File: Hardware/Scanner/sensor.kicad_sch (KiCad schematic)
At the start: 22 parts, among them U1 OPA2376xxD, U4 OPA2376xxD

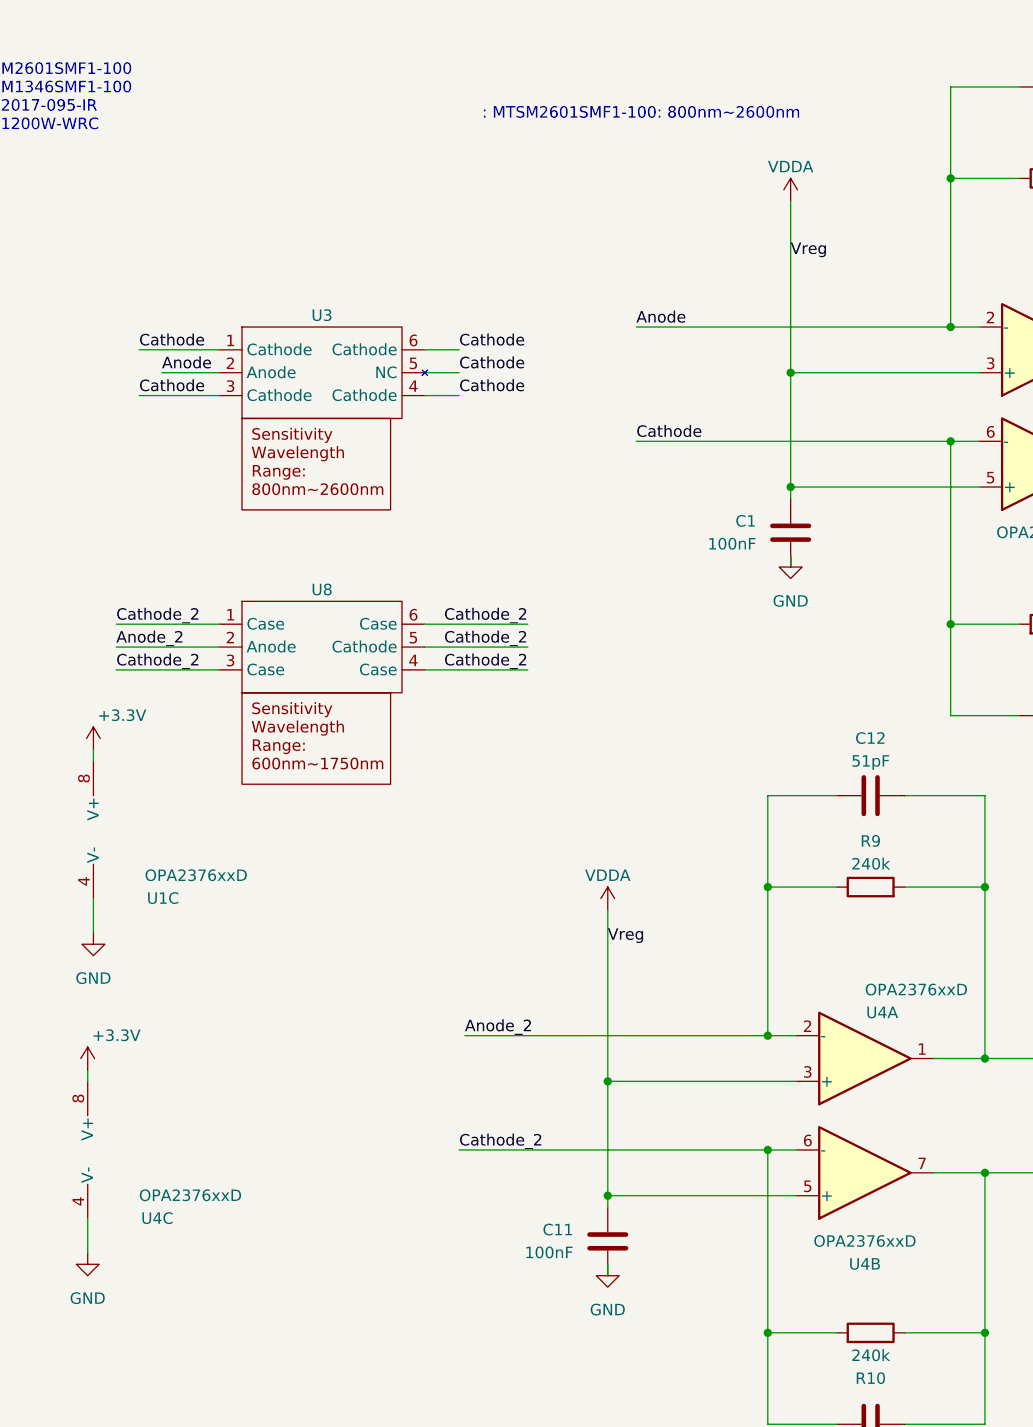
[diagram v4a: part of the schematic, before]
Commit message: updated schematic, and layout, updated bom, fully converted to 3.3v for Voltage input only
Signed-off-by: lokimetasmith <lokimail@gmail.com>
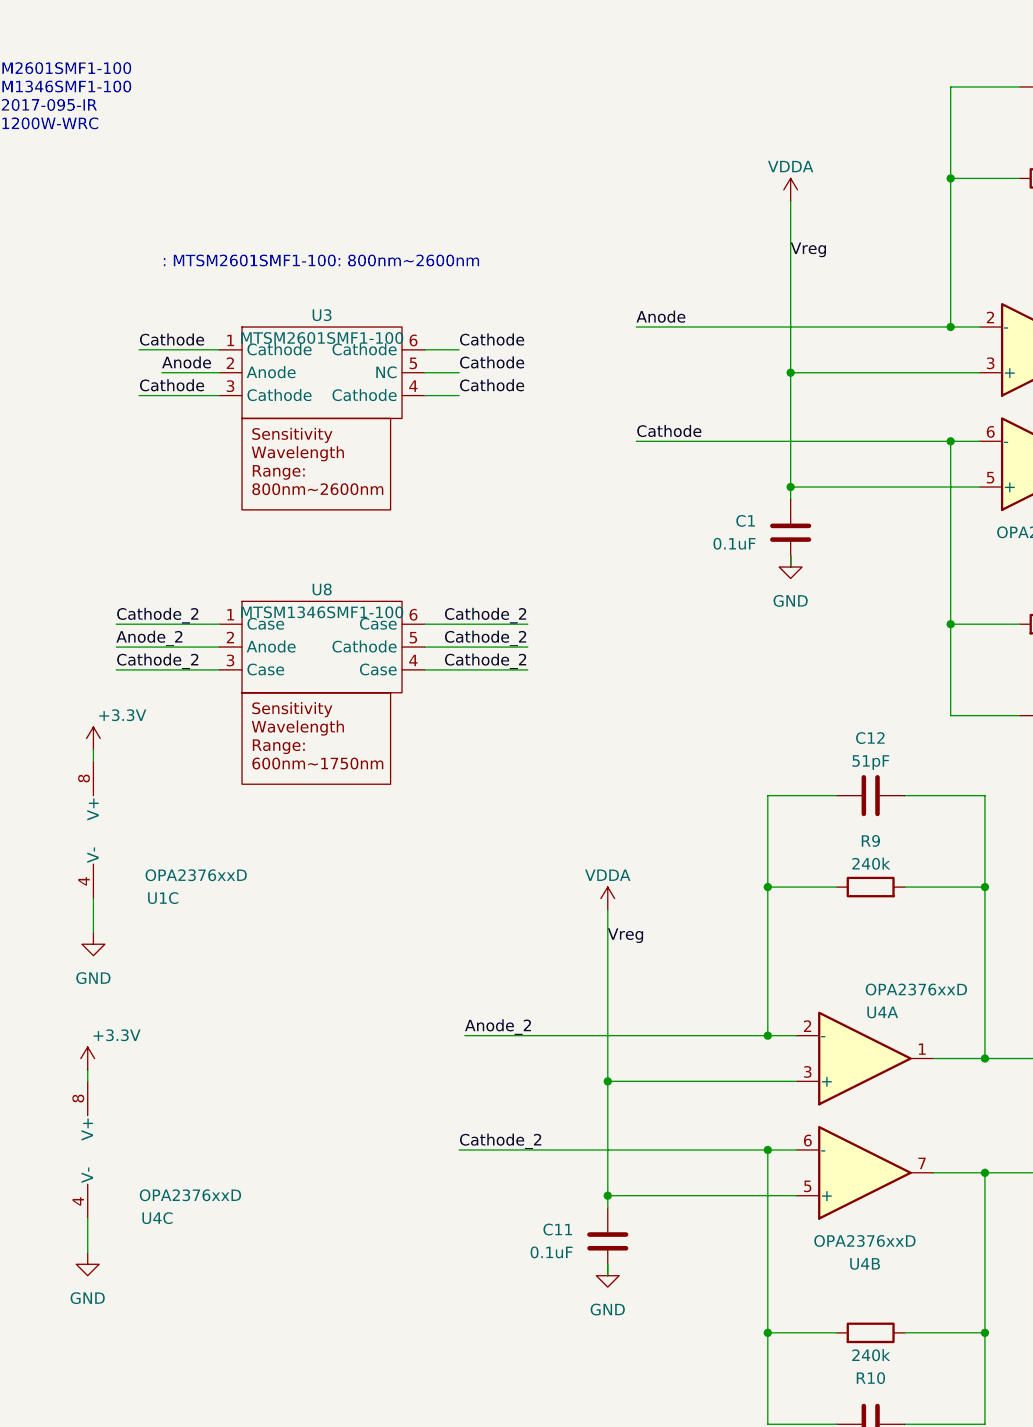
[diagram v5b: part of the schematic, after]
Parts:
- C1, C11: value 100nF -> 0.1uF; digikey description (none) -> CAP CER 0.1UF 16V X7R 0603; digikey part number (none) -> 311-1088-1-ND
- C12, C2, C21, C3: digikey description (none) -> CAP CER 51PF 50V C0G/NP0 0603; digikey part number (none) -> 1276-2310-1-ND
- C22, C4: digikey description (none) -> CAP CER 0.047UF 50V X7R 0603; digikey part number (none) -> 311-4019-1-ND
- C23, C5: digikey description (none) -> CAP CER 100PF 50V C0G/NP0 0603; digikey part number (none) -> 1276-1008-1-ND
- R1, R10, R2, R9: digikey description (none) -> RES 240K OHM 1% 1/10W 0603; digikey part number (none) -> 311-240KHRCT-ND; mouser description (none) -> ERJ-3EKF2403V; mouser part number (none) -> 667-ERJ-3EKF2403V
- R13, R14, R3, R4: digikey description (none) -> RES SMD 301 OHM 1% 1/10W 0603; digikey part number (none) -> P301HCT-ND; mouser description (none) -> ERJ-3EKF3010V; mouser part number (none) -> 667-ERJ-3EKF3010V
- U1, U4: digikey description (none) -> General Purpose Amplifier 2 Circuit Single Ended, Rail-to-R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; mouser description (none) -> OPA2376AIDR; mouser part number (none) -> 595-OPA2376AIDR
- U3: value ~ -> MTSM2601SMF1-100; digikey description (none) -> SENSOR PHOTODIODE 800-2600NM SMD; digikey part number (none) -> 1125-MTSM2601SMF1-100-ND
- U8: value ~ -> MTSM1346SMF1-100; digikey description (none) -> SENSOR PHOTODIODE 1300NM 6SMD; digikey part number (none) -> 1125-MTSM1346SMF1-100-ND

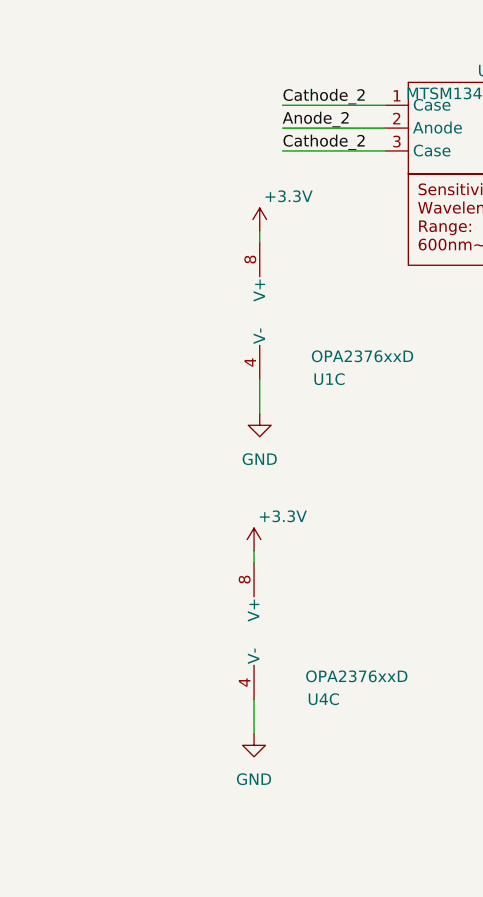
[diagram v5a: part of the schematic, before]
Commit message: added decoupling capactitors, added footprint for 3d model, need to verify new footprint
Signed-off-by: lokimetasmith <lokimail@gmail.com>
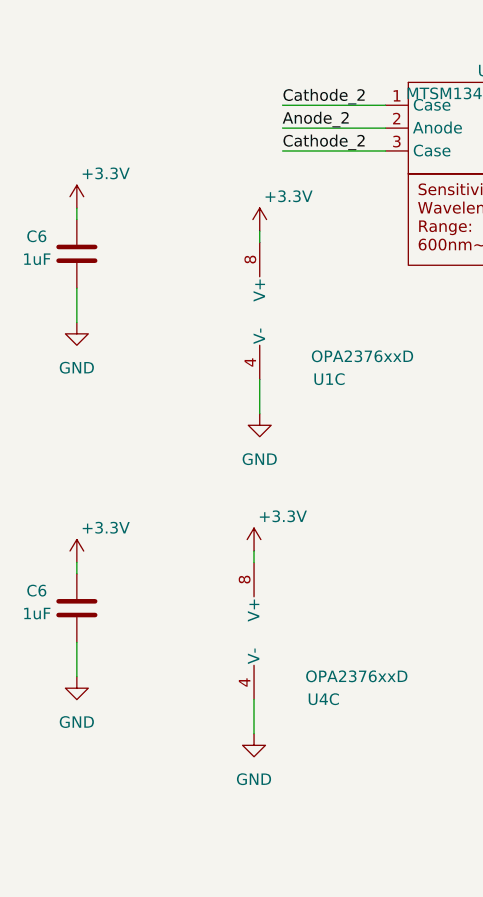
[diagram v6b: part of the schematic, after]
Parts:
- added C6 (x2): 1uF, Capacitor_SMD:C_0603_1608Metric_Pad1.08x0.95mm_HandSolder, symbol Device:C
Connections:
- net +3.3V: now also C6.2, C6.2
- net GND: now also C6.1, C6.1
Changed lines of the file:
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@@
+    (stroke (width 0) (type default))
+  )
+  (wire (pts (xy 17.78 104.14) (xy 17.78 107.95))
     (stroke (width 0) (type default))
   )
@@
     (stroke (width 0) (type default))
   )
+  (wire (pts (xy 17.78 134.62) (xy 17.78 135.89))
+    (stroke (width 0) (type default))
+  )
   (wire (pts (xy 133.35 63.5) (xy 136.525 63.5))
     (stroke (width 0) (type default))
@@
     (stroke (width 0) (type default))
   )
+  (wire (pts (xy 17.78 95.25) (xy 17.78 96.52))
+    (stroke (width 0) (type default))
+  )
   (wire (pts (xy 133.35 83.82) (xy 140.97 83.82))
     (stroke (width 0) (type default))
@@
   )
   (wire (pts (xy 113.03 172.72) (xy 120.65 172.72))
+    (stroke (width 0) (type default))
+  )
+  (wire (pts (xy 17.78 143.51) (xy 17.78 147.32))
     (stroke (width 0) (type default))
   )
@@
     )
   )
+  (symbol (lib_id "Device:C") (at 17.78 100.33 180) (unit 1)
+    (in_bom yes) (on_board yes) (dnp no)
+    (property "Reference" "C6" (at 13.335 98.425 0)
+      (effects (font (size 1.27 1.27)))
+    )
+    (property "Value" "1uF" (at 13.335 100.965 0)
+      (effects (font (size 1.27 1.27)))
+    )
+    (property "Footprint" "Capacitor_SMD:C_0603_1608Metric_Pad1.08x0.95mm_HandSolder" (at 16.8148 96.52 0)
+      (effects (font (size 1.27 1.27)) hide)
+    )
+    (property "Datasheet" "~" (at 17.78 100.33 0)
+      (effects (font (size 1.27 1.27)) hide)
+    )
+    (property "digikey description" "CAP CER 1UF 16V X7R 0603" (at 17.78 100.33 0)
+      (effects (font (size 1.27 1.27)) hide)
+    )
+    (property "digikey part number" "311-1446-1-ND" (at 17.78 100.33 0)
+      (effects (font (size 1.27 1.27)) hide)
+    )
+    (pin "1")
+    (pin "2")
+    (instances
+      (project "RoundScanner"
+        (path "/a818e058-3544-4da8-96fb-1a428660711f/a8dcb7a4-48cf-403e-b881-d44234291c62"
+          (reference "C6") (unit 1)
+        )
+        (path "/a818e058-3544-4da8-96fb-1a428660711f/98df1e87-3735-4cb9-8253-663f6eb2234f"
+          (reference "C24") (unit 1)
+        )
+      )
+    )
+  )
   (symbol (lib_id "Device:R") (at 144.78 83.82 270) (mirror x) (unit 1)
     (in_bom yes) (on_board yes) (dnp no)
@@
         (path "/a818e058-3544-4da8-96fb-1a428660711f/98df1e87-3735-4cb9-8253-663f6eb2234f"
           (reference "R3") (unit 1)
+        )
+      )
+    )
+  )
+  (symbol (lib_id "Device:C") (at 17.78 139.7 180) (unit 1)
+    (in_bom yes) (on_board yes) (dnp no)
+    (property "Reference" "C6" (at 13.335 137.795 0)
+      (effects (font (size 1.27 1.27)))
+    )
+    (property "Value" "1uF" (at 13.335 140.335 0)
+      (effects (font (size 1.27 1.27)))
+    )
+    (property "Footprint" "Capacitor_SMD:C_0603_1608Metric_Pad1.08x0.95mm_HandSolder" (at 16.8148 135.89 0)
+      (effects (font (size 1.27 1.27)) hide)
+    )
+    (property "Datasheet" "~" (at 17.78 139.7 0)
+      (effects (font (size 1.27 1.27)) hide)
+    )
+    (property "digikey description" "CAP CER 1UF 16V X7R 0603" (at 17.78 139.7 0)
+      (effects (font (size 1.27 1.27)) hide)
+    )
+    (property "digikey part number" "311-1446-1-ND" (at 17.78 139.7 0)
+      (effects (font (size 1.27 1.27)) hide)
+    )
+    (pin "1")
+    (pin "2")
+    (instances
+      (project "RoundScanner"
+        (path "/a818e058-3544-4da8-96fb-1a428660711f/a8dcb7a4-48cf-403e-b881-d44234291c62"
+          (reference "C6") (unit 1)
+        )
+        (path "/a818e058-3544-4da8-96fb-1a428660711f/98df1e87-3735-4cb9-8253-663f6eb2234f"
+          (reference "C8") (unit 1)
         )
       )
@@
     )
   )
+  (symbol (lib_id "power:+3.3V") (at 17.78 95.25 0) (unit 1)
+    (in_bom yes) (on_board yes) (dnp no)
+    (property "Reference" "#PWR021" (at 17.78 99.06 0)
+      (effects (font (size 1.27 1.27)) hide)
+    )
+    (property "Value" "+3.3V" (at 20.955 91.44 0)
+      (effects (font (size 1.27 1.27)))
+    )
+    (property "Footprint" "" (at 17.78 95.25 0)
+      (effects (font (size 1.27 1.27)) hide)
+    )
+    (property "Datasheet" "" (at 17.78 95.25 0)
+      (effects (font (size 1.27 1.27)) hide)
+    )
+    (pin "1")
+    (instances
+      (project "RoundScanner"
+        (path "/a818e058-3544-4da8-96fb-1a428660711f/98df1e87-3735-4cb9-8253-663f6eb2234f"
+          (reference "#PWR021") (unit 1)
+        )
+      )
+    )
+  )
+  (symbol (lib_id "power:GND") (at 17.78 107.95 0) (unit 1)
+    (in_bom yes) (on_board yes) (dnp no) (fields_autoplaced)
+    (property "Reference" "#PWR027" (at 17.78 114.3 0)
+      (effects (font (size 1.27 1.27)) hide)
+    )
+    (property "Value" "GND" (at 17.78 113.03 0)
+      (effects (font (size 1.27 1.27)))
+    )
+    (property "Footprint" "" (at 17.78 107.95 0)
+      (effects (font (size 1.27 1.27)) hide)
+    )
+    (property "Datasheet" "" (at 17.78 107.95 0)
+      (effects (font (size 1.27 1.27)) hide)
+    )
+    (pin "1")
+    (instances
+      (project "RoundScanner"
+        (path "/a818e058-3544-4da8-96fb-1a428660711f/98df1e87-3735-4cb9-8253-663f6eb2234f"
+          (reference "#PWR027") (unit 1)
+        )
+      )
+    )
+  )
   (symbol (lib_id "power:GND") (at 95.25 154.94 0) (unit 1)
     (in_bom yes) (on_board yes) (dnp no) (fields_autoplaced)
@@
         (path "/a818e058-3544-4da8-96fb-1a428660711f/98df1e87-3735-4cb9-8253-663f6eb2234f"
           (reference "#PWR09") (unit 1)
+        )
+      )
+    )
+  )
+  (symbol (lib_id "power:+3.3V") (at 17.78 134.62 0) (unit 1)
+    (in_bom yes) (on_board yes) (dnp no)
+    (property "Reference" "#PWR024" (at 17.78 138.43 0)
+      (effects (font (size 1.27 1.27)) hide)
+    )
+    (property "Value" "+3.3V" (at 20.955 130.81 0)
+      (effects (font (size 1.27 1.27)))
+    )
+    (property "Footprint" "" (at 17.78 134.62 0)
+      (effects (font (size 1.27 1.27)) hide)
+    )
+    (property "Datasheet" "" (at 17.78 134.62 0)
+      (effects (font (size 1.27 1.27)) hide)
+    )
+    (pin "1")
+    (instances
+      (project "RoundScanner"
+        (path "/a818e058-3544-4da8-96fb-1a428660711f/98df1e87-3735-4cb9-8253-663f6eb2234f"
+          (reference "#PWR024") (unit 1)
         )
       )
@@
         )
       )
+    )
+  )
+  (symbol (lib_id "power:GND") (at 17.78 147.32 0) (unit 1)
+    (in_bom yes) (on_board yes) (dnp no) (fields_autoplaced)
+    (property "Reference" "#PWR025" (at 17.78 153.67 0)
+      (effects (font (size 1.27 1.27)) hide)
+    )
+    (property "Value" "GND" (at 17.78 152.4 0)
+      (effects (font (size 1.27 1.27)))
+    )
+    (property "Footprint" "" (at 17.78 147.32 0)
+      (effects (font (size 1.27 1.27)) hide)
+    )
+    (property "Datasheet" "" (at 17.78 147.32 0)
+      (effects (font (size 1.27 1.27)) hide)
+    )
+    (pin "1")
+    (instances
+      (project "RoundScanner"
+        (path "/a818e058-3544-4da8-96fb-1a428660711f/98df1e87-3735-4cb9-8253-663f6eb2234f"
+          (reference "#PWR025") (unit 1)
+        )
+      )
